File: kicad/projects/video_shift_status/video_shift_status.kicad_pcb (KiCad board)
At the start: 2 copper layers, 203.2 x 97.8 mm, 47 parts, among them J1 peripheral_addr_bus_connector, J2 peripheral_aux_connector, J3 peripheral_membank_connector, J4 Conn_01x16_Socket, J5 Conn_01x16_Socket, J6 video_aux, J7 Conn_01x03_Pin, J8 Conn_01x04_Socket, J9 Conn_02x06_Odd_Even, U1 74HC245, U10 74HC377, U11 74HC138, U12 74HC04, U13 74HC10, U14 74HC04, U2 74HC245, U3 74HC245, U4 74HC245, U5 74HC245, U6 74HC245, U7 74HC245, U8 74HC245, U9 74HC245

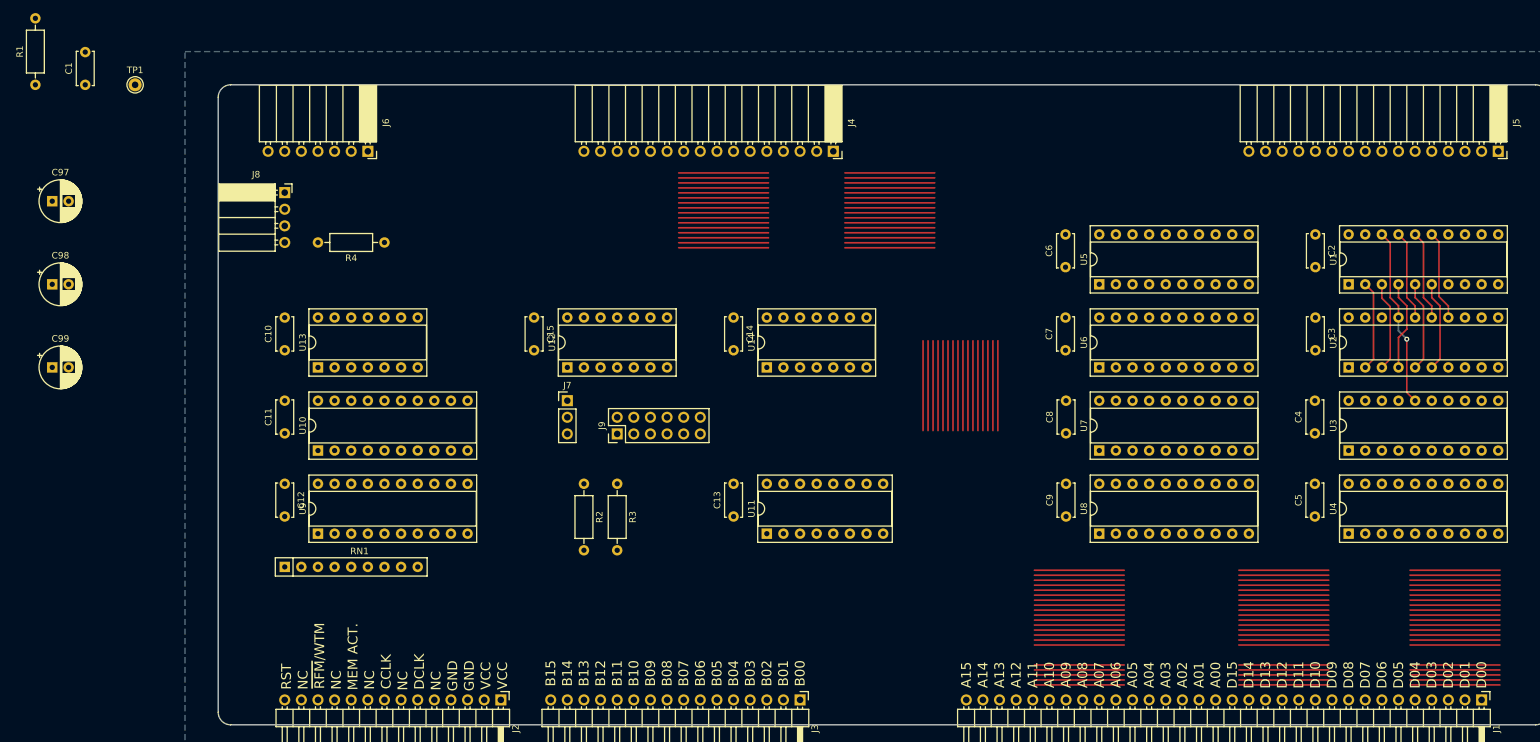
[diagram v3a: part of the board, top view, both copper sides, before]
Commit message: Start work on shift status delay PCB.
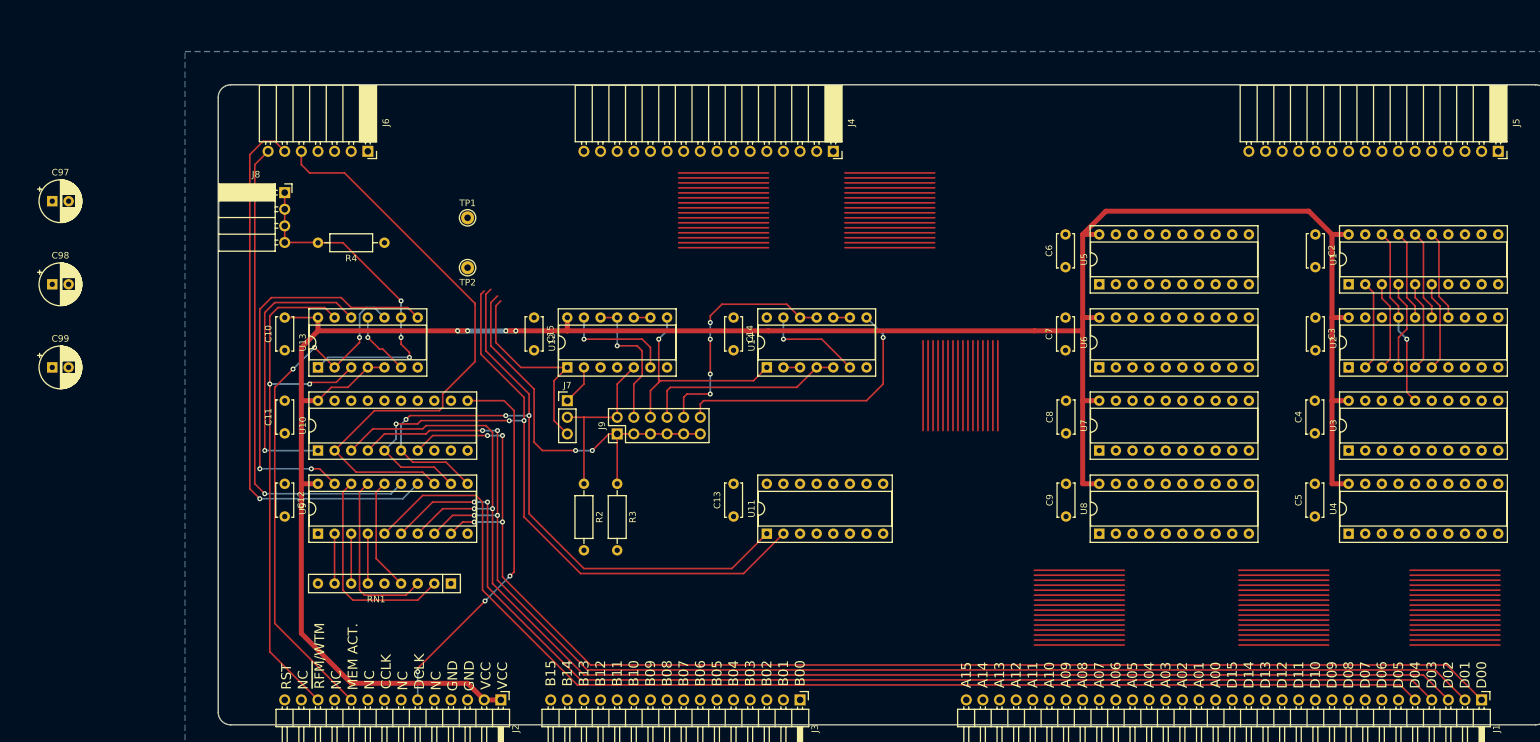
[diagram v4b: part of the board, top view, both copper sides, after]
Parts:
- removed C1: C, Capacitor_THT:C_Disc_D5.0mm_W2.5mm_P5.00mm
- removed R1: R_US, Resistor_THT:R_Axial_DIN0207_L6.3mm_D2.5mm_P10.16mm_Horizontal
- added TP2: Shift Sel 1, Connector_Pin:Pin_D1.0mm_L10.0mm, F.Cu at (88.9, 78.7)
- TP1: value TestPoint -> Shift Sel 0
- moved TP1 54.7 mm to (88.9, 71.1)
- moved RN1 25.5 mm to (86.4, 127.0), turned to 180 degrees
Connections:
- RN1 pad 6: unconnected-(RN1-R5-Pad6) -> Net-(RN1-R5)
- RN1 pad 9: Net-(RN1-R8) -> unconnected-(RN1-R8-Pad9)
- TP1 pad 1: unconnected-(TP1-Pad1) -> /SHIFT_SEL_0
- U1 pad 1: unconnected-(U1-DIR-Pad1) -> GND
- U14 pad 12: /PIX_CLK_DELAY_5 -> /PIX_CLK_DELAY_4
- U14 pad 13: Net-(U14-Pad10) -> Net-(U14-Pad13)
- U14 pad 6: Net-(U14-Pad6) -> Net-(U14-Pad13)
- U14 pad 8: /PIX_CLK_DELAY_4 -> /PIX_CLK_DELAY_5
- U14 pad 9: Net-(U14-Pad6) -> Net-(U14-Pad10)
- U2 pad 1: unconnected-(U2-DIR-Pad1) -> GND
- U3 pad 1: unconnected-(U3-DIR-Pad1) -> GND
- U4 pad 1: unconnected-(U4-DIR-Pad1) -> GND
- U5 pad 1: unconnected-(U5-DIR-Pad1) -> GND
- U6 pad 1: unconnected-(U6-DIR-Pad1) -> GND
- U7 pad 1: unconnected-(U7-DIR-Pad1) -> GND
- U8 pad 1: unconnected-(U8-DIR-Pad1) -> GND
- U9 pad 16: Net-(RN1-R8) -> Net-(RN1-R3)
- U9 pad 17: Net-(RN1-R7) -> Net-(RN1-R2)
- U9 pad 18: Net-(RN1-R6) -> Net-(RN1-R1)
- U9 pad 2: Net-(RN1-R3) -> Net-(RN1-R7)
- U9 pad 3: Net-(RN1-R2) -> Net-(RN1-R6)
- U9 pad 4: Net-(RN1-R1) -> Net-(RN1-R5)
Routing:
- net VCC: track 0.00 -> 365.9 mm, vias 0 -> 4
- net /DATA_BUS_02: track 41.1 -> 213.1 mm, vias 0 -> 2
- net /DATA_BUS_01: track 41.1 -> 210.1 mm, vias 0 -> 4
- net /DATA_BUS_00: track 41.1 -> 201.5 mm, vias 0 -> 4
- net /DATA_BUS_04: track 41.1 -> 180.7 mm
- net /DATA_BUS_03: track 41.1 -> 179.6 mm, vias 0 -> 2
- net /SHIFT_SEL_1: track 0.00 -> 120.1 mm, vias 0 -> 3
- net /SHIFT_SEL_0: track 0.00 -> 115.7 mm, vias 0 -> 3
- net /BANK_SEL: track 0.00 -> 92.0 mm
- net /~{RFM}/WTM: track 0.00 -> 86.3 mm, vias 0 -> 2
- net /H_BLANK: track 0.00 -> 85.1 mm, vias 0 -> 1
- net /MEM_ACT: track 0.00 -> 80.1 mm, vias 0 -> 3
- net /V_BLANK: track 0.00 -> 75.3 mm, vias 0 -> 1
- net /~{READ}: track 0.00 -> 62.9 mm, vias 0 -> 2
- net /PIX_CLK_MOD: track 0.00 -> 60.1 mm, vias 0 -> 2
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
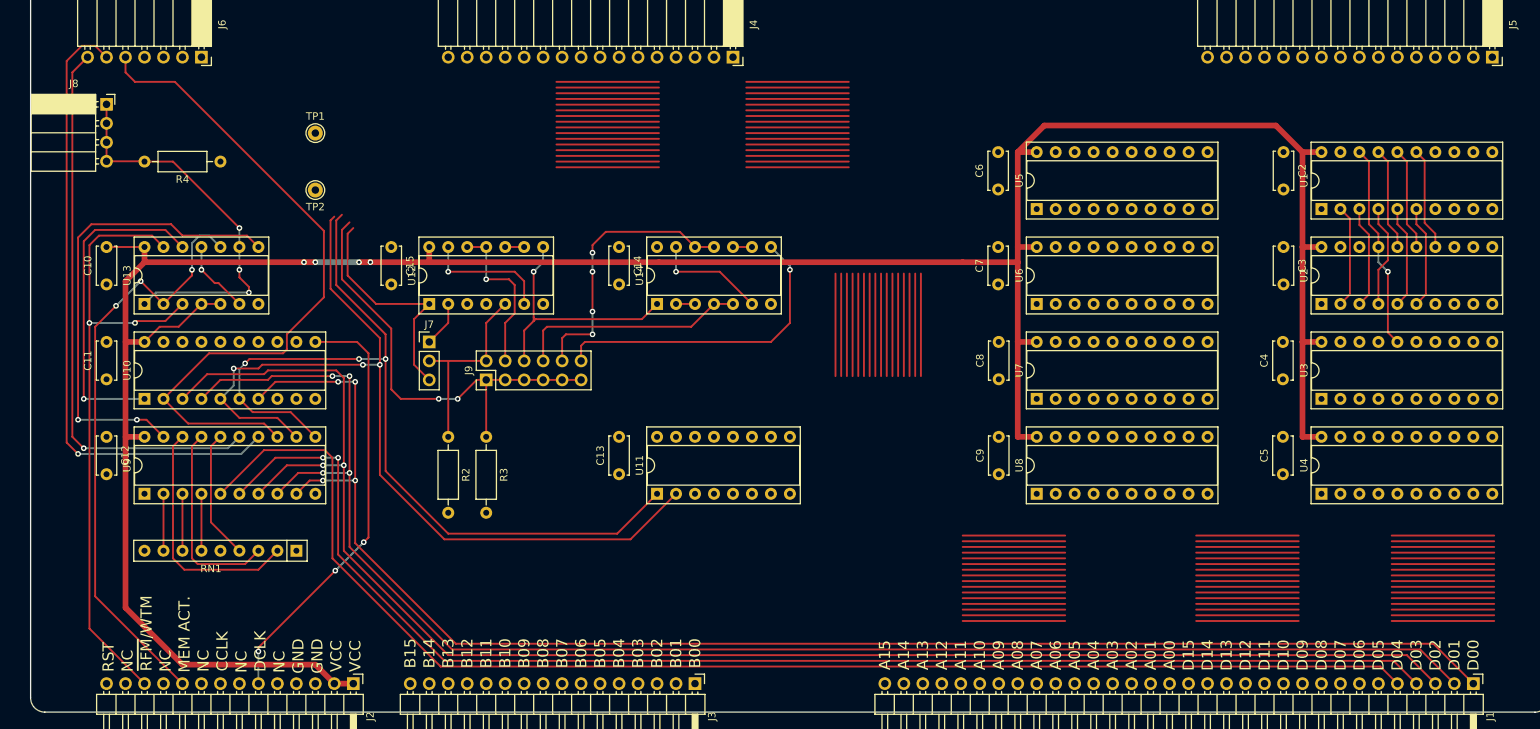
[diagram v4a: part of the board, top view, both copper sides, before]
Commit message: Most of work for shift status delay PCB complete.
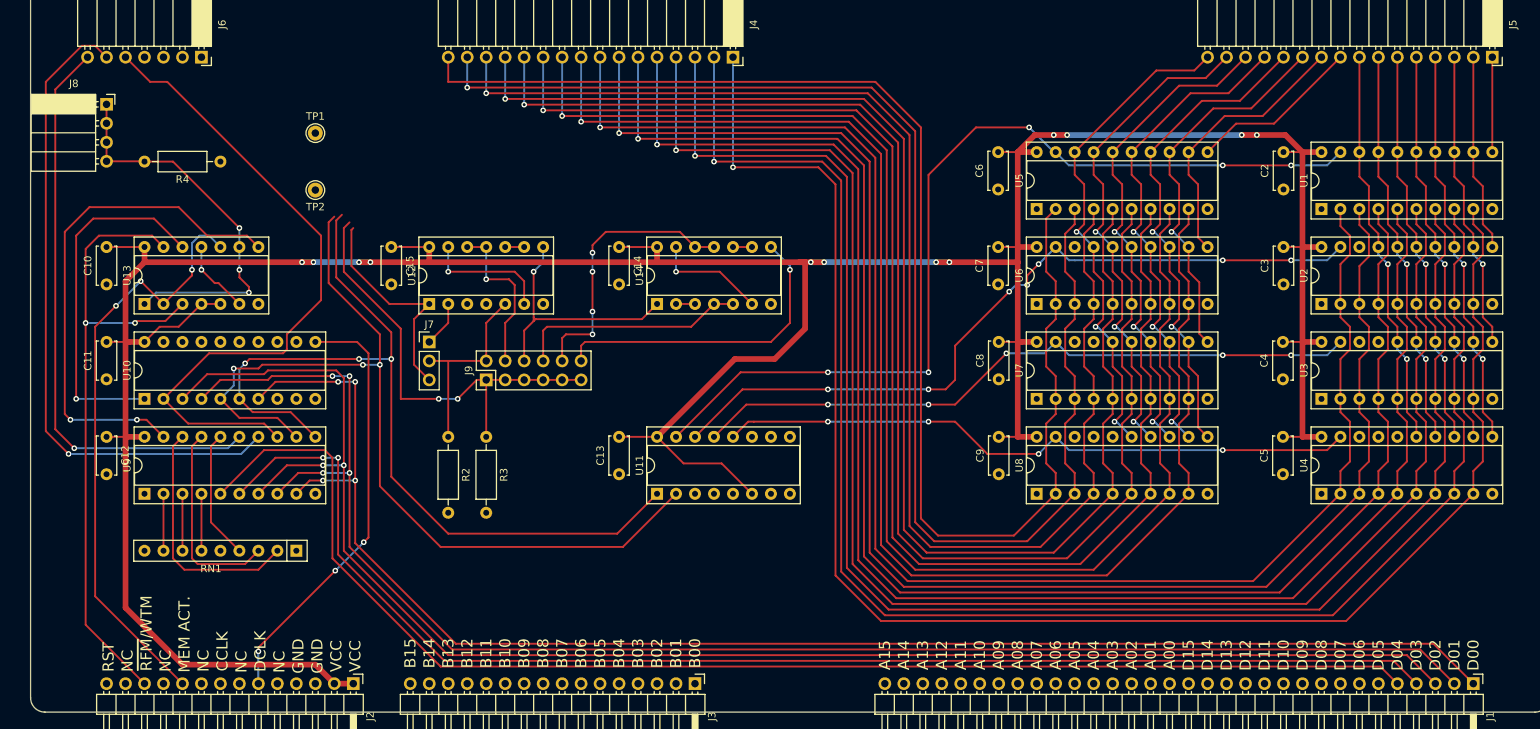
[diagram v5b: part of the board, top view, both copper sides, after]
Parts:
- moved C2 5.00 mm to (218.4, 78.7), turned to 90 degrees
- moved C3 5.00 mm to (218.4, 91.4), turned to 90 degrees
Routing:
- net /ROW_OUT_0: track 82.3 -> 217.9 mm, vias 0 -> 1
- net /ROW_OUT_1: track 82.3 -> 216.8 mm, vias 0 -> 1
- net /ROW_OUT_2: track 82.3 -> 215.7 mm, vias 0 -> 1
- net /~{SHIFT_0}: track 0.00 -> 124.4 mm, vias 0 -> 5
- net /ROW_OUT_3: track 96.0 -> 214.7 mm, vias 0 -> 1
- net /ROW_OUT_4: track 96.0 -> 213.6 mm, vias 0 -> 1
- net /ROW_OUT_5: track 96.0 -> 212.5 mm, vias 0 -> 1
- net /ROW_OUT_6: track 96.0 -> 211.4 mm, vias 0 -> 1
- net /ROW_OUT_7: track 96.0 -> 210.3 mm, vias 0 -> 1
- net /COL_OUT_0: track 82.3 -> 191.5 mm, vias 0 -> 1
- net /COL_OUT_1: track 82.3 -> 190.4 mm, vias 0 -> 1
- net /COL_OUT_2: track 82.3 -> 189.3 mm, vias 0 -> 1
- net /COL_OUT_3: track 82.3 -> 188.3 mm, vias 0 -> 1
- net /COL_OUT_4: track 82.3 -> 187.2 mm, vias 0 -> 1
- net /COL_OUT_5: track 82.3 -> 186.1 mm, vias 0 -> 1
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
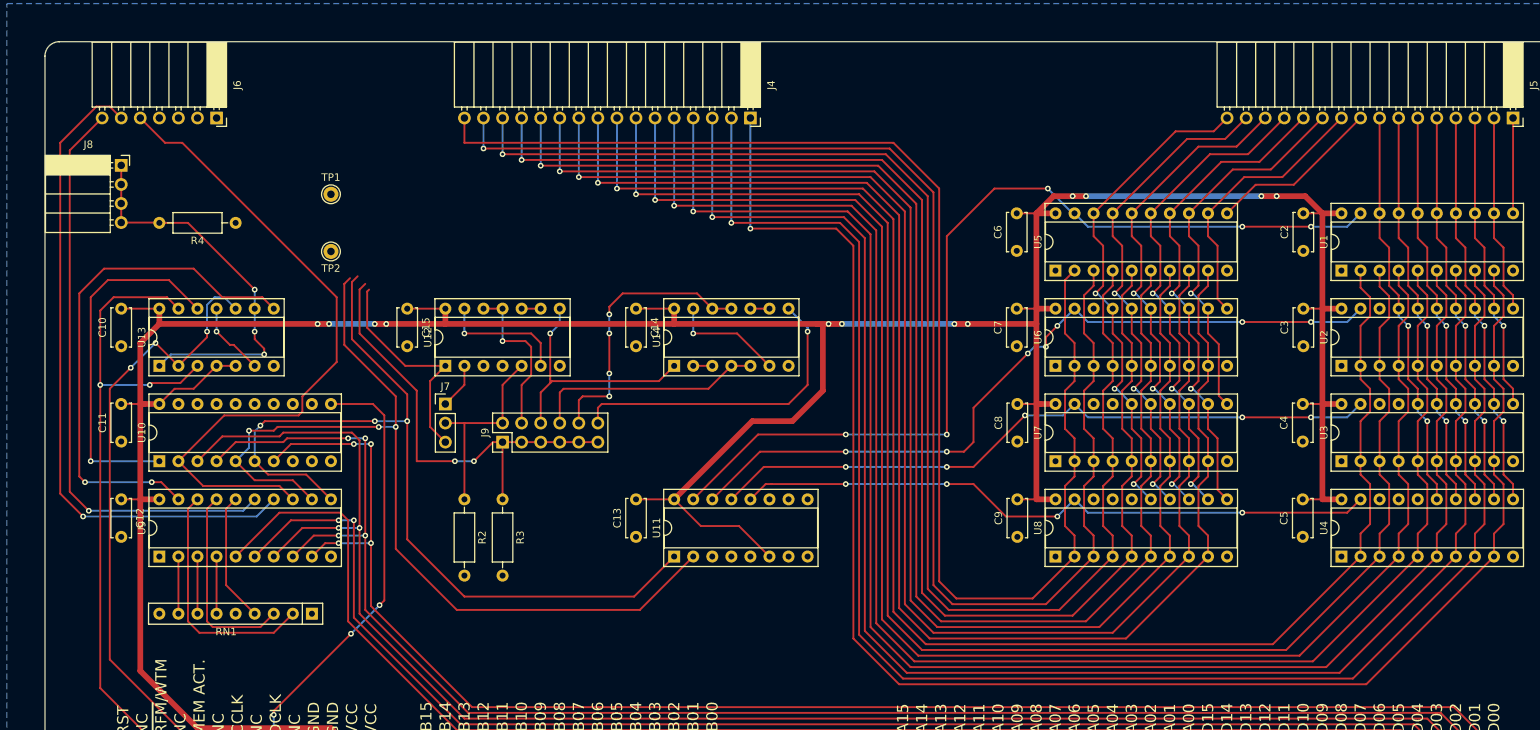
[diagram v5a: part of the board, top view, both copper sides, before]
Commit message: Add indicator LEDs to shift status delay board. Bit of work on bank sel PCB.
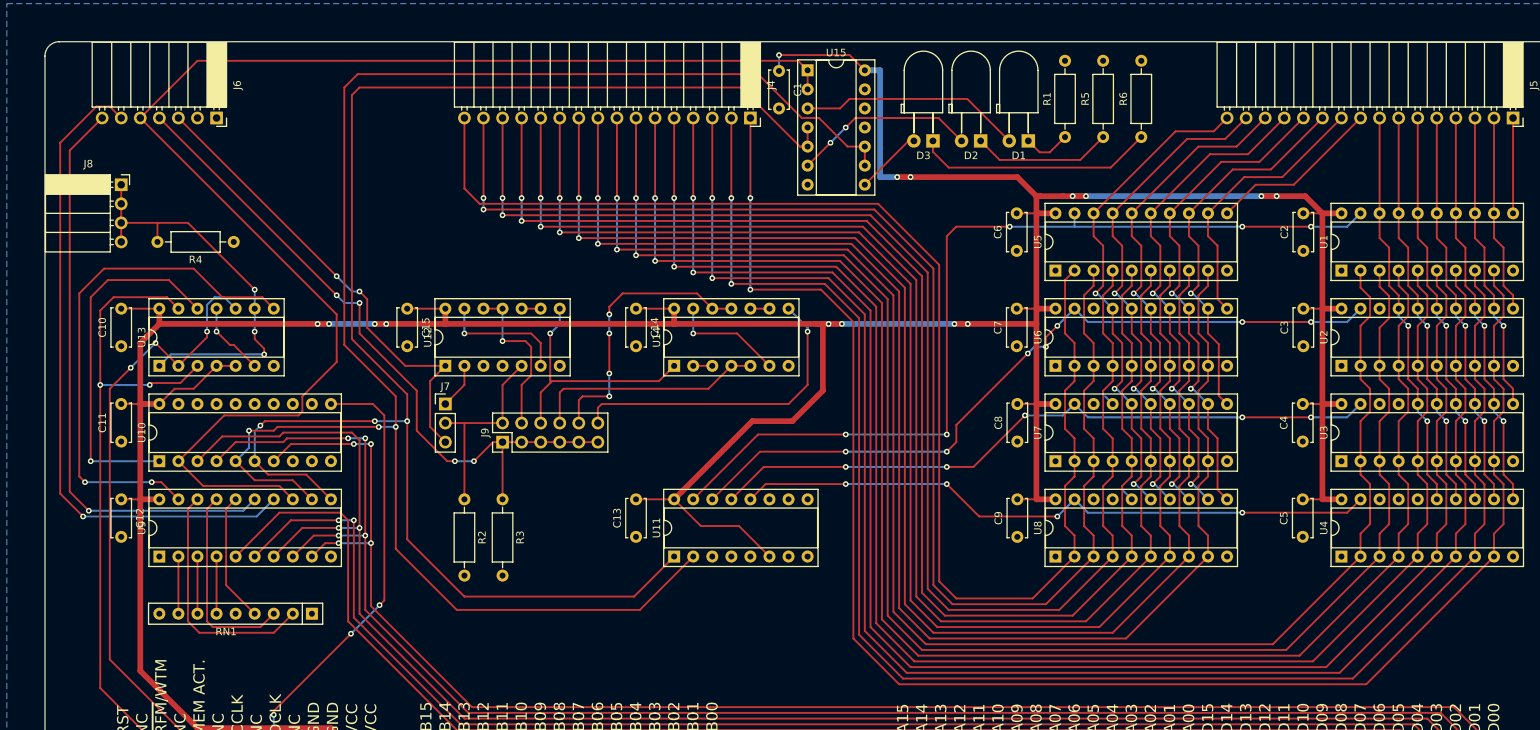
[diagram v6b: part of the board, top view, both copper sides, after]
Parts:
- removed TP1: Shift Sel 0, Connector_Pin:Pin_D1.0mm_L10.0mm
- removed TP2: Shift Sel 1, Connector_Pin:Pin_D1.0mm_L10.0mm
- added C1: C, Capacitor_THT:C_Disc_D5.0mm_W2.5mm_P5.00mm, F.Cu at (148.6, 54.7)
- added D1: LED, sixteen-bit-computer:LED_D5.0mm_Horizontal_O3.81mm_Z3.0mm, F.Cu at (181.8, 64.0)
- added D2: LED, sixteen-bit-computer:LED_D5.0mm_Horizontal_O3.81mm_Z3.0mm, F.Cu at (175.5, 64.0)
- added D3: LED, sixteen-bit-computer:LED_D5.0mm_Horizontal_O3.81mm_Z3.0mm, F.Cu at (169.1, 64.0)
- added R1: R_US, Resistor_THT:R_Axial_DIN0207_L6.3mm_D2.5mm_P10.16mm_Horizontal, F.Cu at (186.7, 63.5)
- added R5: R_US, Resistor_THT:R_Axial_DIN0207_L6.3mm_D2.5mm_P10.16mm_Horizontal, F.Cu at (191.8, 63.5)
- added R6: R_US, Resistor_THT:R_Axial_DIN0207_L6.3mm_D2.5mm_P10.16mm_Horizontal, F.Cu at (196.8, 63.5)
- added U15: 74HC08, Package_DIP:DIP-14_W7.62mm_Socket, F.Cu at (152.4, 54.6)
- moved J8 2.58 mm to (61.0, 69.8)
- moved R4 2.55 mm to (75.9, 77.5)
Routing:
- net /SHIFT_SEL_1: track 122.0 -> 223.7 mm
- net /BANK_SEL: track 89.8 -> 183.6 mm
- net /SHIFT_SEL_0: track 116.5 -> 207.2 mm
- net VCC: track 467.5 -> 523.2 mm, vias 12 -> 15
- net /PIX_CLK_RAW: track 29.5 -> 63.3 mm, vias 0 -> 2
- net Net-(D3-K): track 0.00 -> 31.8 mm
- net /PIX_CLK_MOD: track 59.9 -> 91.5 mm, vias 2 -> 4
- net /BANK_SEL_LED: track 0.00 -> 29.7 mm
- net /SHIFT_SEL_0_LED: track 0.00 -> 24.4 mm, vias 0 -> 2
- net Net-(D2-K): track 0.00 -> 18.6 mm
- net /SHIFT_SEL_1_LED: track 0.00 -> 8.96 mm
- net Net-(D1-K): track 0.00 -> 6.36 mm
- net GND: track 0.00 -> 3.23 mm
- net /ADDRESSED: track 52.8 -> 55.4 mm
- net /~{SHIFT_0}: track 124.4 -> 121.9 mm
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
